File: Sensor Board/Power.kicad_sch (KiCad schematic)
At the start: 21 parts

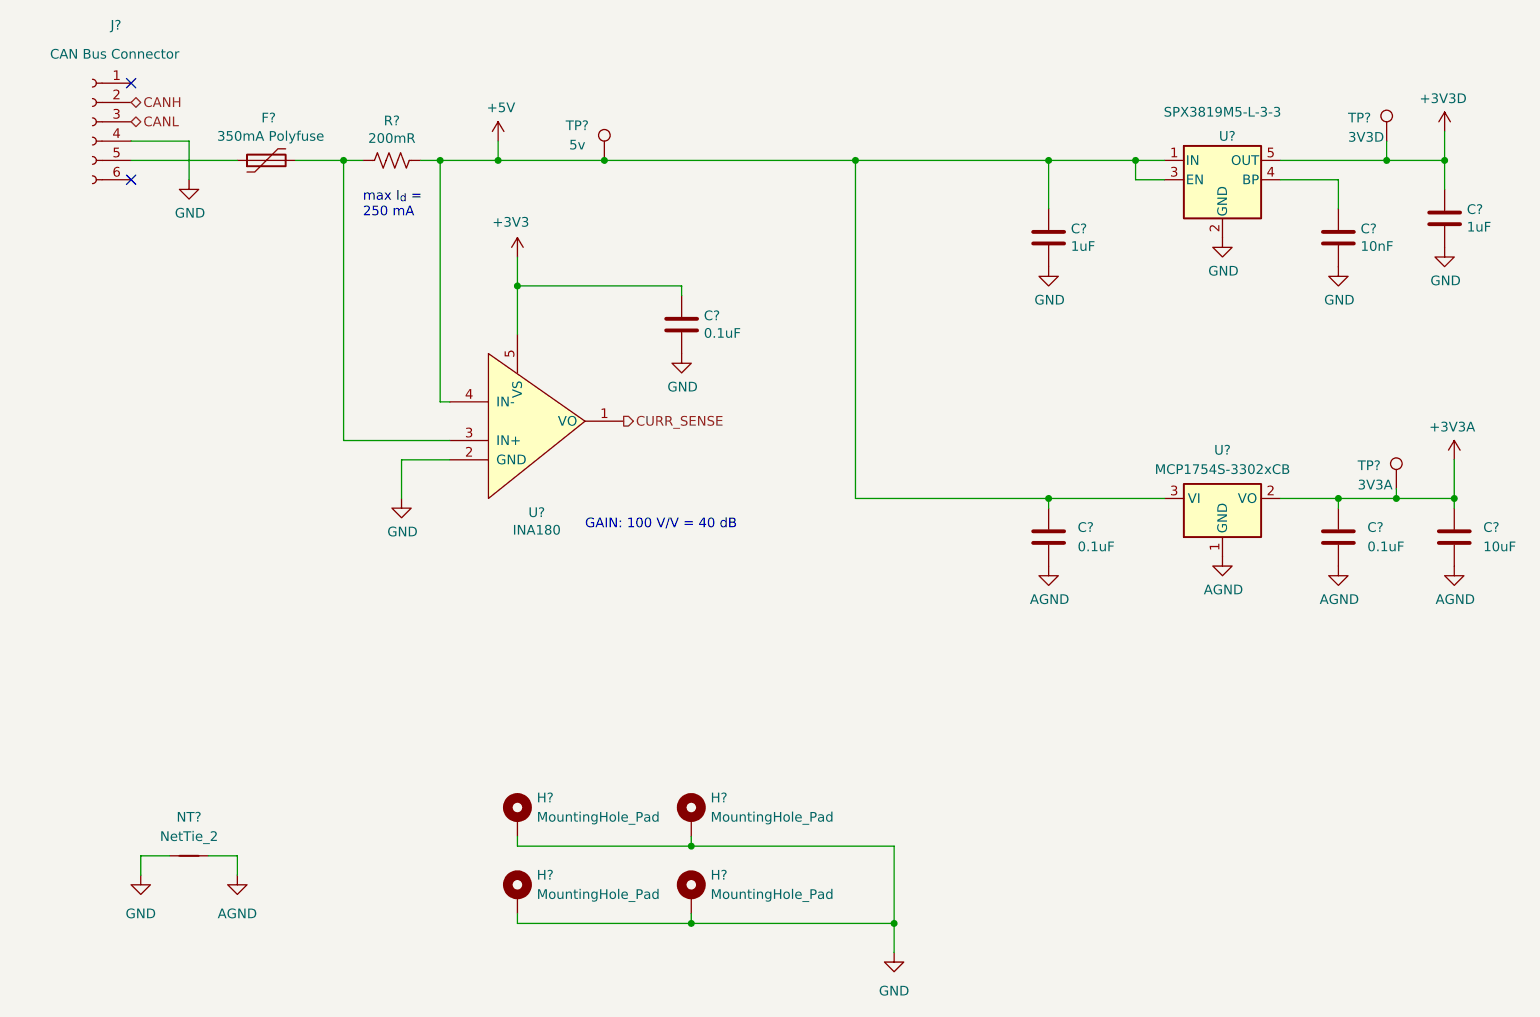
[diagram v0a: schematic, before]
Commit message: added footprints. Custom footprint for photodiode
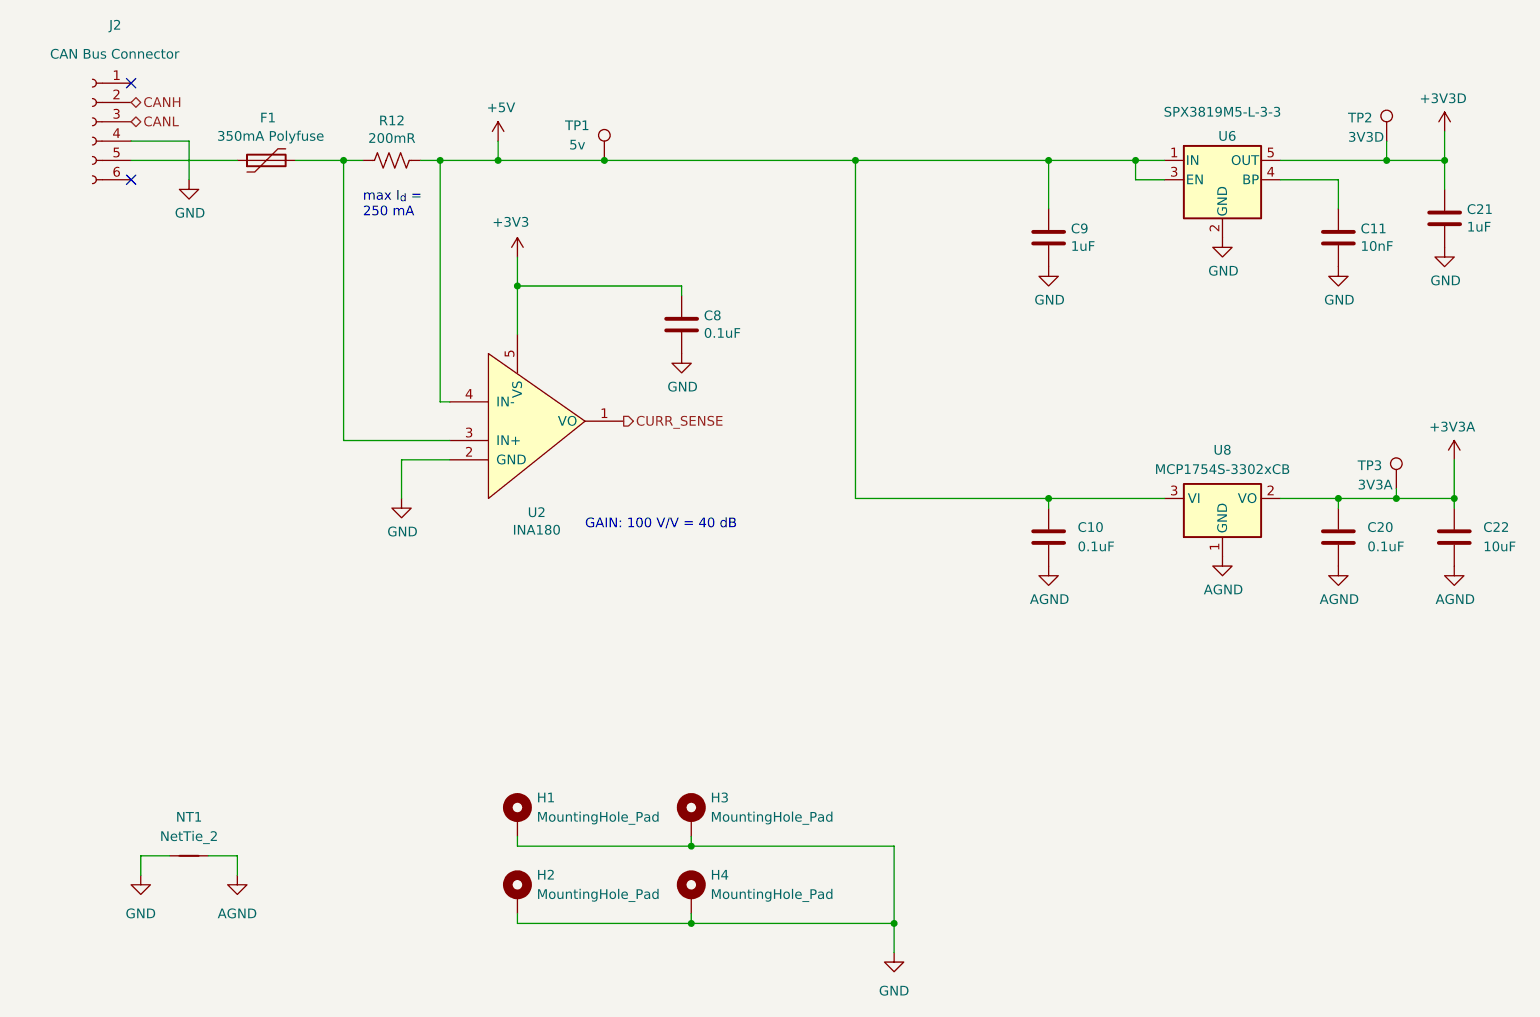
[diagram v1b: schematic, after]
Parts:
- C10, C20, C22: renamed from C?; footprint (none) -> Capacitor_SMD:C_0805_2012Metric_Pad1.18x1.45mm_HandSolder
- gave numbers to parts that had none: 18
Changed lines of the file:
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@@
 		(on_board yes)
 		(dnp no)
-		(property "Reference" "H?"
+		(property "Reference" "H3"
 			(at 125.73 134.6199 0)
 			(effects
@@
 			(project "Sensor Board"
 				(path "/82a9869f-36b9-4173-b7be-dd71d5b66335/53f15c84-d39c-4951-aa92-80979a6364f3"
-					(reference "H?")
+					(reference "H3")
 					(unit 1)
 				)
@@
 		(on_board yes)
 		(dnp no)
-		(property "Reference" "C?"
+		(property "Reference" "C9"
 			(at 173.101 59.7916 0)
 			(effects
@@
 			(project "Sensor Board"
 				(path "/82a9869f-36b9-4173-b7be-dd71d5b66335/53f15c84-d39c-4951-aa92-80979a6364f3"
-					(reference "C?")
+					(reference "C9")
 					(unit 1)
 				)
@@
 		(dnp no)
 		(fields_autoplaced yes)
-		(property "Reference" "C?"
+		(property "Reference" "C20"
 			(at 212.09 99.0599 0)
 			(effects
@@
 			)
 		)
-		(property "Footprint" ""
+		(property "Footprint" "Capacitor_SMD:C_0805_2012Metric_Pad1.18x1.45mm_HandSolder"
 			(at 209.2452 104.14 0)
 			(effects
@@
 			(project "Sensor Board"
 				(path "/82a9869f-36b9-4173-b7be-dd71d5b66335/53f15c84-d39c-4951-aa92-80979a6364f3"
-					(reference "C?")
+					(reference "C20")
 					(unit 1)
 				)
@@
 		(on_board yes)
 		(dnp no)
-		(property "Reference" "C?"
+		(property "Reference" "C11"
 			(at 211.201 59.7916 0)
 			(effects
@@
 			(project "Sensor Board"
 				(path "/82a9869f-36b9-4173-b7be-dd71d5b66335/53f15c84-d39c-4951-aa92-80979a6364f3"
-					(reference "C?")
+					(reference "C11")
 					(unit 1)
 				)
@@
 		(dnp no)
 		(fields_autoplaced yes)
-		(property "Reference" "U?"
+		(property "Reference" "U8"
 			(at 193.04 88.9 0)
 			(effects
@@
 			(project ""
 				(path "/82a9869f-36b9-4173-b7be-dd71d5b66335/53f15c84-d39c-4951-aa92-80979a6364f3"
-					(reference "U?")
+					(reference "U8")
 					(unit 1)
 				)
@@
 		(dnp no)
 		(fields_autoplaced yes)
-		(property "Reference" "NT?"
+		(property "Reference" "NT1"
 			(at 57.15 137.16 0)
 			(effects
@@
 			(project "Sensor Board"
 				(path "/82a9869f-36b9-4173-b7be-dd71d5b66335/53f15c84-d39c-4951-aa92-80979a6364f3"
-					(reference "NT?")
+					(reference "NT1")
 					(unit 1)
 				)
@@
 		(dnp no)
 		(fields_autoplaced yes)
-		(property "Reference" "H?"
+		(property "Reference" "H4"
 			(at 125.73 144.7799 0)
 			(effects
@@
 			(project "Sensor Board"
 				(path "/82a9869f-36b9-4173-b7be-dd71d5b66335/53f15c84-d39c-4951-aa92-80979a6364f3"
-					(reference "H?")
+					(reference "H4")
 					(unit 1)
 				)
@@
 		(on_board yes)
 		(dnp no)
-		(property "Reference" "J?"
+		(property "Reference" "J2"
 			(at 48.26 33.02 0)
 			(effects
@@
 			(project "Sensor Board"
 				(path "/82a9869f-36b9-4173-b7be-dd71d5b66335/53f15c84-d39c-4951-aa92-80979a6364f3"
-					(reference "J?")
+					(reference "J2")
 					(unit 1)
 				)
@@
 		(on_board yes)
 		(dnp no)
-		(property "Reference" "U?"
+		(property "Reference" "U2"
 			(at 102.87 97.1042 0)
 			(effects
@@
 			(project "Sensor Board"
 				(path "/82a9869f-36b9-4173-b7be-dd71d5b66335/53f15c84-d39c-4951-aa92-80979a6364f3"
-					(reference "U?")
+					(reference "U2")
 					(unit 1)
 				)
@@
 		(on_board yes)
 		(dnp no)
-		(property "Reference" "TP?"
+		(property "Reference" "TP1"
 			(at 108.204 46.228 0)
 			(effects
@@
 			(project "Sensor Board"
 				(path "/82a9869f-36b9-4173-b7be-dd71d5b66335/53f15c84-d39c-4951-aa92-80979a6364f3"
-					(reference "TP?")
+					(reference "TP1")
 					(unit 1)
 				)
@@
 		(dnp no)
 		(fields_autoplaced yes)
-		(property "Reference" "C?"
+		(property "Reference" "C10"
 			(at 173.99 99.0599 0)
 			(effects
@@
 			)
 		)
-		(property "Footprint" ""
+		(property "Footprint" "Capacitor_SMD:C_0805_2012Metric_Pad1.18x1.45mm_HandSolder"
 			(at 171.1452 104.14 0)
 			(effects
@@
 			(project ""
 				(path "/82a9869f-36b9-4173-b7be-dd71d5b66335/53f15c84-d39c-4951-aa92-80979a6364f3"
-					(reference "C?")
+					(reference "C10")
 					(unit 1)
 				)
@@
 		(on_board yes)
 		(dnp no)
-		(property "Reference" "H?"
+		(property "Reference" "H2"
 			(at 102.87 144.7799 0)
 			(effects
@@
 			(project "Sensor Board"
 				(path "/82a9869f-36b9-4173-b7be-dd71d5b66335/53f15c84-d39c-4951-aa92-80979a6364f3"
-					(reference "H?")
+					(reference "H2")
 					(unit 1)
 				)
@@
 		(on_board yes)
 		(dnp no)
-		(property "Reference" "TP?"
+		(property "Reference" "TP2"
 			(at 209.55 45.212 0)
 			(effects
@@
 			(project "Sensor Board"
 				(path "/82a9869f-36b9-4173-b7be-dd71d5b66335/53f15c84-d39c-4951-aa92-80979a6364f3"
-					(reference "TP?")
+					(reference "TP2")
 					(unit 1)
 				)
@@
 		(dnp no)
 		(fields_autoplaced yes)
-		(property "Reference" "C?"
+		(property "Reference" "C22"
 			(at 227.33 99.0599 0)
 			(effects
@@
 			)
 		)
-		(property "Footprint" ""
+		(property "Footprint" "Capacitor_SMD:C_0805_2012Metric_Pad1.18x1.45mm_HandSolder"
 			(at 224.4852 104.14 0)
 			(effects
@@
 			(project "Sensor Board"
 				(path "/82a9869f-36b9-4173-b7be-dd71d5b66335/53f15c84-d39c-4951-aa92-80979a6364f3"
-					(reference "C?")
+					(reference "C22")
 					(unit 1)
 				)
@@
 		(on_board yes)
 		(dnp no)
-		(property "Reference" "R?"
+		(property "Reference" "R12"
 			(at 83.82 45.593 90)
 			(effects
@@
 			(project "Sensor Board"
 				(path "/82a9869f-36b9-4173-b7be-dd71d5b66335/53f15c84-d39c-4951-aa92-80979a6364f3"
-					(reference "R?")
+					(reference "R12")
 					(unit 1)
 				)
@@
 		(on_board yes)
 		(dnp no)
-		(property "Reference" "C?"
+		(property "Reference" "C21"
 			(at 225.171 57.2516 0)
 			(effects
@@
 			(project "Sensor Board"
 				(path "/82a9869f-36b9-4173-b7be-dd71d5b66335/53f15c84-d39c-4951-aa92-80979a6364f3"
-					(reference "C?")
+					(reference "C21")
 					(unit 1)
 				)
@@
 		(on_board yes)
 		(dnp no)
-		(property "Reference" "TP?"
+		(property "Reference" "TP3"
 			(at 210.82 90.932 0)
 			(effects
@@
 			(project "Sensor Board"
 				(path "/82a9869f-36b9-4173-b7be-dd71d5b66335/53f15c84-d39c-4951-aa92-80979a6364f3"
-					(reference "TP?")
+					(reference "TP3")
 					(unit 1)
 				)
@@
 		(on_board yes)
 		(dnp no)
-		(property "Reference" "H?"
+		(property "Reference" "H1"
 			(at 102.87 134.6199 0)
 			(effects
@@
 			(project "Sensor Board"
 				(path "/82a9869f-36b9-4173-b7be-dd71d5b66335/53f15c84-d39c-4951-aa92-80979a6364f3"
-					(reference "H?")
+					(reference "H1")
 					(unit 1)
 				)
@@
 		(on_board yes)
 		(dnp no)
-		(property "Reference" "U?"
+		(property "Reference" "U6"
 			(at 193.675 47.625 0)
 			(effects
@@
 			(project "Sensor Board"
 				(path "/82a9869f-36b9-4173-b7be-dd71d5b66335/53f15c84-d39c-4951-aa92-80979a6364f3"
-					(reference "U?")
+					(reference "U6")
 					(unit 1)
 				)
@@
 		(on_board yes)
 		(dnp no)
-		(property "Reference" "F?"
+		(property "Reference" "F1"
 			(at 68.58 45.212 90)
 			(effects
@@
 			(project "Sensor Board"
 				(path "/82a9869f-36b9-4173-b7be-dd71d5b66335/53f15c84-d39c-4951-aa92-80979a6364f3"
-					(reference "F?")
+					(reference "F1")
 					(unit 1)
 				)
@@
 		(on_board yes)
 		(dnp no)
-		(property "Reference" "C?"
+		(property "Reference" "C8"
 			(at 124.841 71.2216 0)
 			(effects
@@
 			(project "Sensor Board"
 				(path "/82a9869f-36b9-4173-b7be-dd71d5b66335/53f15c84-d39c-4951-aa92-80979a6364f3"
-					(reference "C?")
-					(unit 1)
-				)
+					(reference "C8")
+					(unit 1)
+				)

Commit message: fixed footprints not loading
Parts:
- J2: footprint Canhw:connector_Harwin_G125–MG10605M4P -> canhw:connector_Harwin_G125–MG10605M4P
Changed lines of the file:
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@@
 			)
 		)
-		(property "Footprint" "Canhw:connector_Harwin_G125–MG10605M4P"
+		(property "Footprint" "canhw:connector_Harwin_G125–MG10605M4P"
 			(at 44.45 45.72 0)
 			(effects

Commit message: did layout
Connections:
- net +3V3 is gone; now on net +3V3D: C8.1, U2.5 (VS)
- net AGND: now also H1.1
- net GND: no longer H1.1
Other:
- moved on the sheet: H1
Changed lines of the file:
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@@
 	)
 	(junction
-		(at 123.19 140.97)
-		(diameter 0)
-		(color 0 0 0 0)
-	)
-	(junction
 		(at 144.78 50.8)
 		(diameter 0)
@@
 	(wire
 		(pts
-			(xy 100.33 139.7) (xy 100.33 140.97)
+			(xy 93.98 139.7) (xy 93.98 142.24)
 		)
 		(stroke
@@
 	(wire
 		(pts
-			(xy 100.33 140.97) (xy 123.19 140.97)
-		)
-		(stroke
-			(width 0)
-			(type default)
-		)
-	)
-	(wire
-		(pts
 			(xy 200.66 50.8) (xy 214.63 50.8)
 		)
@@
 			)
 		)
-		(property "Value" "+3V3"
+		(property "Value" "+3V3D"
 			(at 97.028 58.928 0)
 			(effects
@@
 	(symbol
 		(lib_id "Mechanical:MountingHole_Pad")
-		(at 100.33 137.16 0)
+		(at 93.98 137.16 0)
 		(unit 1)
 		(exclude_from_sim no)
@@
 		(dnp no)
 		(property "Reference" "H1"
-			(at 102.87 134.6199 0)
+			(at 96.52 134.6199 0)
 			(effects
 				(font
@@
 		)
 		(property "Value" "MountingHole_Pad"
-			(at 102.87 137.1599 0)
+			(at 96.52 137.1599 0)
 			(effects
 				(font
@@
 		)
 		(property "Footprint" "MountingHole:MountingHole_3.2mm_M3_DIN965_Pad"
-			(at 100.33 137.16 0)
+			(at 93.98 137.16 0)
 			(effects
 				(font
@@
 		)
 		(property "Datasheet" "~"
-			(at 100.33 137.16 0)
+			(at 93.98 137.16 0)
 			(effects
 				(font
@@
 		)
 		(property "Description" ""
-			(at 100.33 137.16 0)
+			(at 93.98 137.16 0)
 			(effects
 				(font
@@
 					(unit 1)
 				)
+			)
+		)
+	)
+	(symbol
+		(lib_id "power:GND")
+		(at 93.98 142.24 0)
+		(unit 1)
+		(exclude_from_sim no)
+		(in_bom yes)
+		(on_board yes)
+		(dnp no)
+		(fields_autoplaced yes)
+		(property "Reference" "#PWR11"
+			(at 93.98 148.59 0)
+			(effects
+				(font
+					(size 1.27 1.27)
+				)
+				(hide yes)
+			)
+		)
+		(property "Value" "AGND"
+			(at 93.98 147.32 0)
+			(effects
+				(font
+					(size 1.27 1.27)
+				)
+			)
+		)
+		(property "Footprint" ""
+			(at 93.98 142.24 0)
+			(effects
+				(font
+					(size 1.27 1.27)
+				)
+				(hide yes)
+			)
+		)
+		(property "Datasheet" ""
+			(at 93.98 142.24 0)
+			(effects
+				(font
+					(size 1.27 1.27)
+				)
+				(hide yes)
+			)
+		)
+		(property "Description" "Power symbol creates a global label with name \"GND\" , ground"
+			(at 93.98 142.24 0)
+			(effects
+				(font
+					(size 1.27 1.27)
+				)
+				(hide yes)
+			)
+		)
+		(pin "1"
+		)
+		(instances
+			(project "Sensor Board"
+				(path "/82a9869f-36b9-4173-b7be-dd71d5b66335/53f15c84-d39c-4951-aa92-80979a6364f3"
+					(reference "#PWR11")
+					(unit 1)
+				)

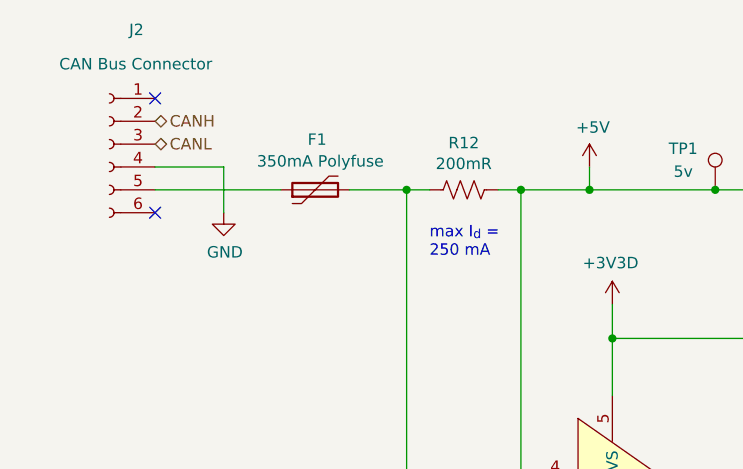
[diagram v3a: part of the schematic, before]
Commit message: implemented Joe's comments
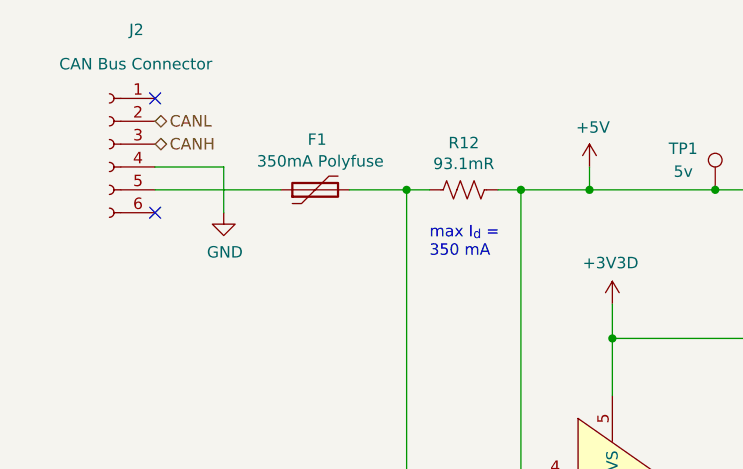
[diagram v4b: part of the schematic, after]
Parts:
- R12: value 200mR -> 93.1mR
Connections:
- net CANH: now also J2.3 (Pin_3); no longer J2.2 (Pin_2)
- net CANL: now also J2.2 (Pin_2); no longer J2.3 (Pin_3)
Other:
- note added: "max I_{d} = 350 mA"
- note removed: "max I_{d} = 250 mA"
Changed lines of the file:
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@@
 		)
 	)
-	(text "max I_{d} =\n250 mA"
+	(text "max I_{d} =\n350 mA"
 		(exclude_from_sim no)
 		(at 80.01 58.42 0)
@@
 	(hierarchical_label "CANL"
 		(shape bidirectional)
-		(at 49.53 45.72 0)
+		(at 49.53 43.18 0)
 		(effects
 			(font
@@
 	(hierarchical_label "CANH"
 		(shape bidirectional)
-		(at 49.53 43.18 0)
+		(at 49.53 45.72 0)
 		(effects
 			(font
@@
 			)
 		)
-		(property "Value" "200mR"
+		(property "Value" "93.1mR"
 			(at 83.82 47.9044 90)
 			(effects
